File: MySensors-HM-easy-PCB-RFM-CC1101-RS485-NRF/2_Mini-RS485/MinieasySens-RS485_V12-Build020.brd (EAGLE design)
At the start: 63 x 33 mm, 38 parts, among them IC1 ATSHA204A, IC2 REG1117, IC4 REG1117, M1 ARDUINO-PRO-MINI-3.3V#NP, X1 1751264, X4 1751264

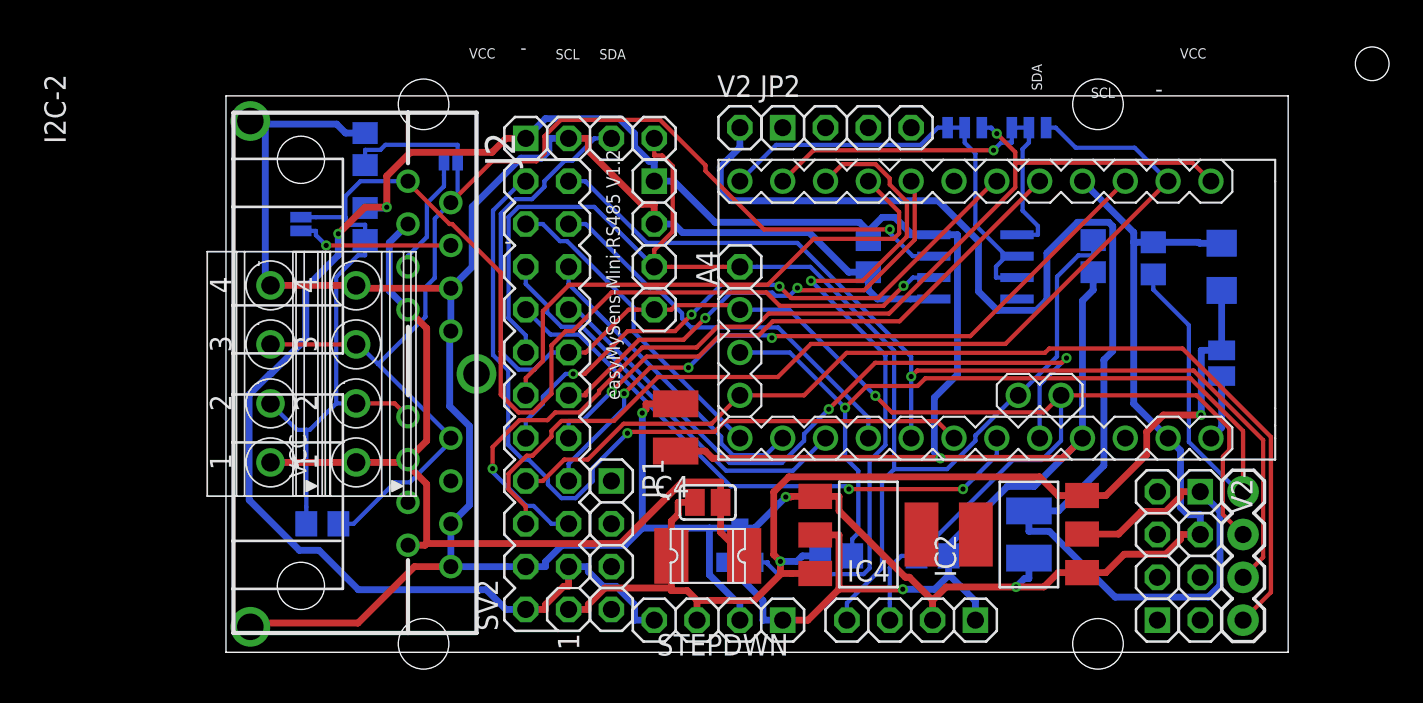
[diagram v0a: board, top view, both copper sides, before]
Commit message: BluePill, MiniRS485 Sensor+Gateway
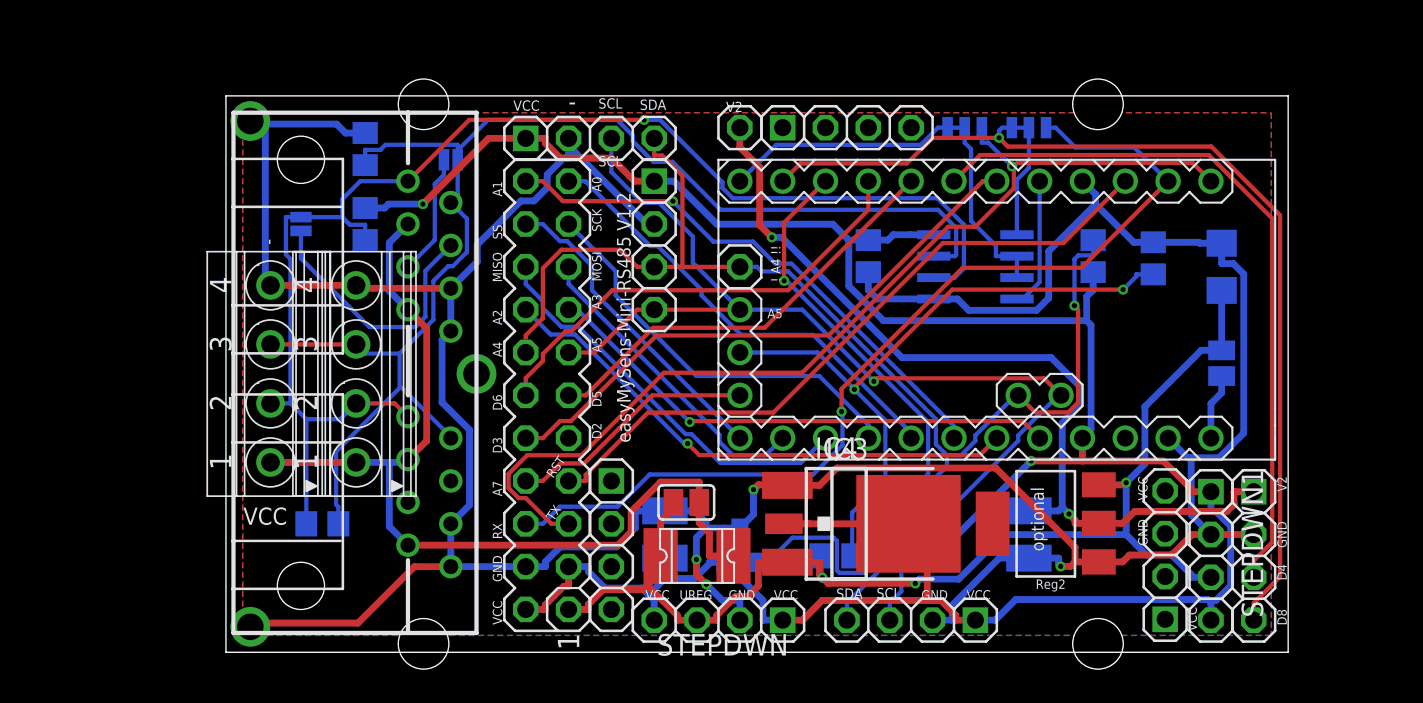
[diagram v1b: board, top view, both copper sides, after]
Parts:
- removed OPT1: (no value), SparkFun-Connectors:1X04
- added IC3: LD117ADT50TR, v-reg:DPACK
- added STEPDWN1: (no value), pinhead-2:1X04-S
- IC4: value REG1117 -> LM1117MPX-ADJ; device burr-brown:SOT223 -> lm1117:SOT223
- moved C4 6.38 mm to (26.0, 6.99), flipped to the bottom
- moved V2- 3.18 mm to (61.0, 5.71)
- moved IC4 2.01 mm to (36.2, 7.62)
- moved RAW1 1.27 mm to (27.3, 8.89)
- moved IC2 1.18 mm to (48.6, 7.62)
- moved F1 0.63 mm to (27.9, 5.71)
- moved JP4 0.46 mm to (55.7, 5.76)
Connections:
- removed net DI: RS485.4
- new net D2_INT0: M1.J7.8, RS485.4
- net A0: no longer OPT1.2
- net A5: no longer OPT1.3
- net A6: no longer OPT1.4
- net A7: no longer OPT1.1
- net D2: no longer M1.J7.8
- net D4: now also V2-.3
- net D8: now also V2-.4
- net GND: now also IC3.1, STEPDWN1.2
- net UREG: now also IC3.3, STEPDWN1.3
- net VCC: now also IC3.4, IC4.TAB, STEPDWN1.1, STEPDWN1.4
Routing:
- net A7: track 61.2 -> 14.8 mm
- net D8: track 15.4 -> 58.4 mm
- net D4: track 0.00 -> 42.8 mm
- net D2: track 34.8 -> 0.00 mm, vias 1 -> 0
- net A0: track 60.8 -> 27.0 mm, vias 1 -> 0
- net V2: track 84.7 -> 52.0 mm, vias 0 -> 2
- net A5: track 92.5 -> 64.7 mm
- net VCC: track 181.6 -> 159.3 mm, vias 4 -> 2
- net A6: track 61.3 -> 39.8 mm, vias 1 -> 2
- net A1: track 47.7 -> 32.1 mm
- net A3: track 41.5 -> 31.1 mm, vias 2 -> 1
- net D2_INT0: track 0.00 -> 7.75 mm
- net 4: track 9.40 -> 15.8 mm, vias 1 -> 0
- net GND: track 198.6 -> 204.9 mm, vias 3 -> 4
- net D6: track 32.3 -> 27.4 mm
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- added copper zone on layer 1, net GND
- added copper zone on layer 16, net GND
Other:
- board text added: "! A4 !!"
- board text added: "120"
- board text added: "A0"
- board text added: "A1"
- board text added: "A2"
- board text added: "A3"
- board text added: "A4"
- board text added: "A5"
- board text added: "A7"
- board text added: "Bus Pull"
- board text added: "Bus Terminat."
- board text added: "C1"
- board text added: "C10"
- board text added: "C6"
- board text added: "Crypto"
- board text added: "D2"
- board text added: "D3"
- board text added: "D4"
- board text added: "D5"
- board text added: "D6"
- board text added: "D8"
- board text added: "GND"
- board text added: "MISO"
- board text added: "MOSI"
- board text added: "R1"
- board text added: "R2"
- board text added: "R3"
- board text added: "R7"
- board text added: "RAW"
- board text added: "RST"
- board text added: "RX"
- board text added: "Reg2"
- board text added: "SCK"
- board text added: "SS"
- board text added: "TX"
- board text added: "UREG"
- board text added: "V2"
- board text added: "easyMySens-RS485-Mini V1.2"
- board text added: "optional"
- board text removed: "HW"
- board text removed: "SW"
- board text removed: "easyMySens-Mini V0.2"
